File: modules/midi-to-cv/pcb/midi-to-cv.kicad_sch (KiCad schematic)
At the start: 47 parts, among them U2 ATtiny4313-PU

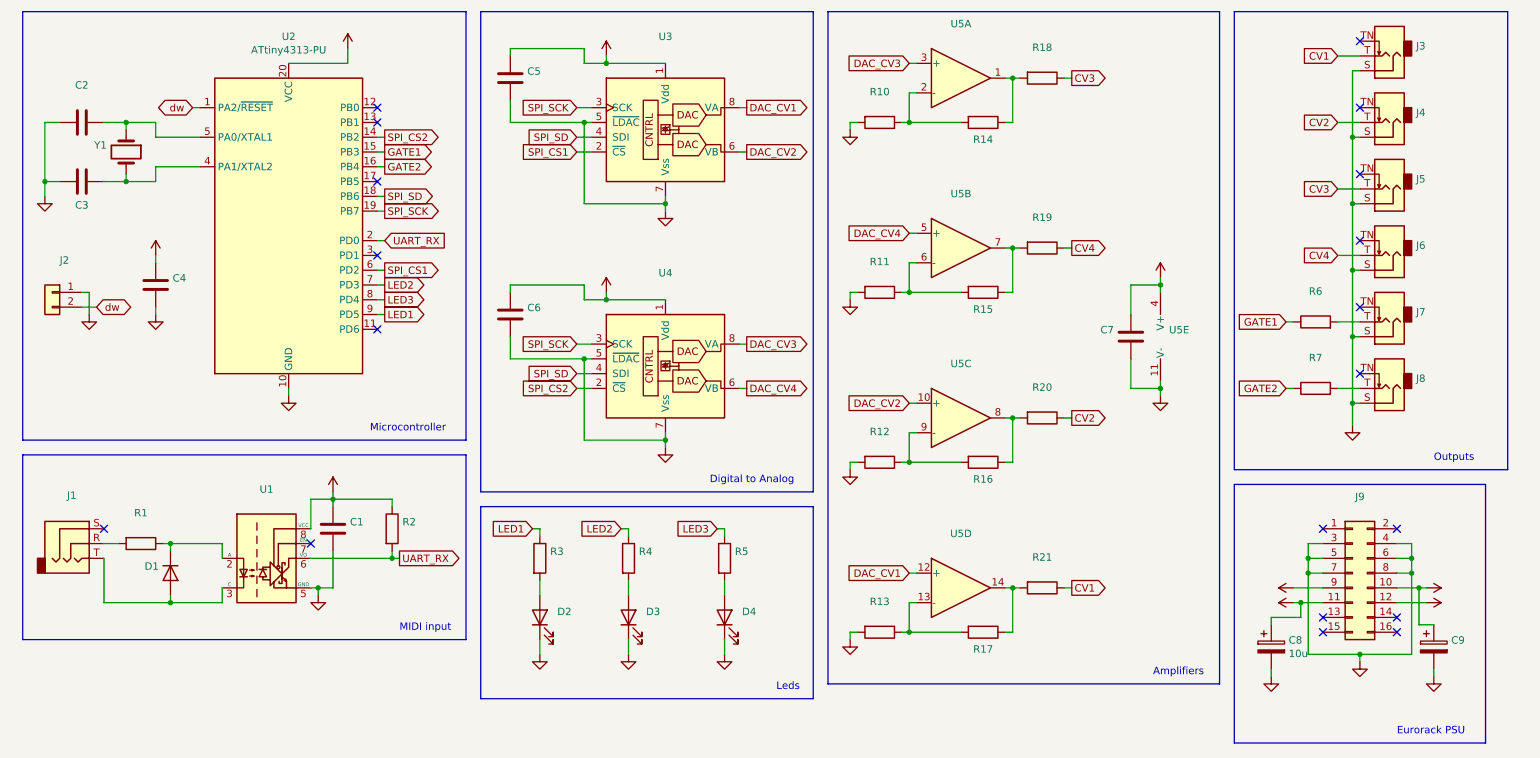
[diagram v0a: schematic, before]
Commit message: modules: midi-to-cv: revision A (redesign)
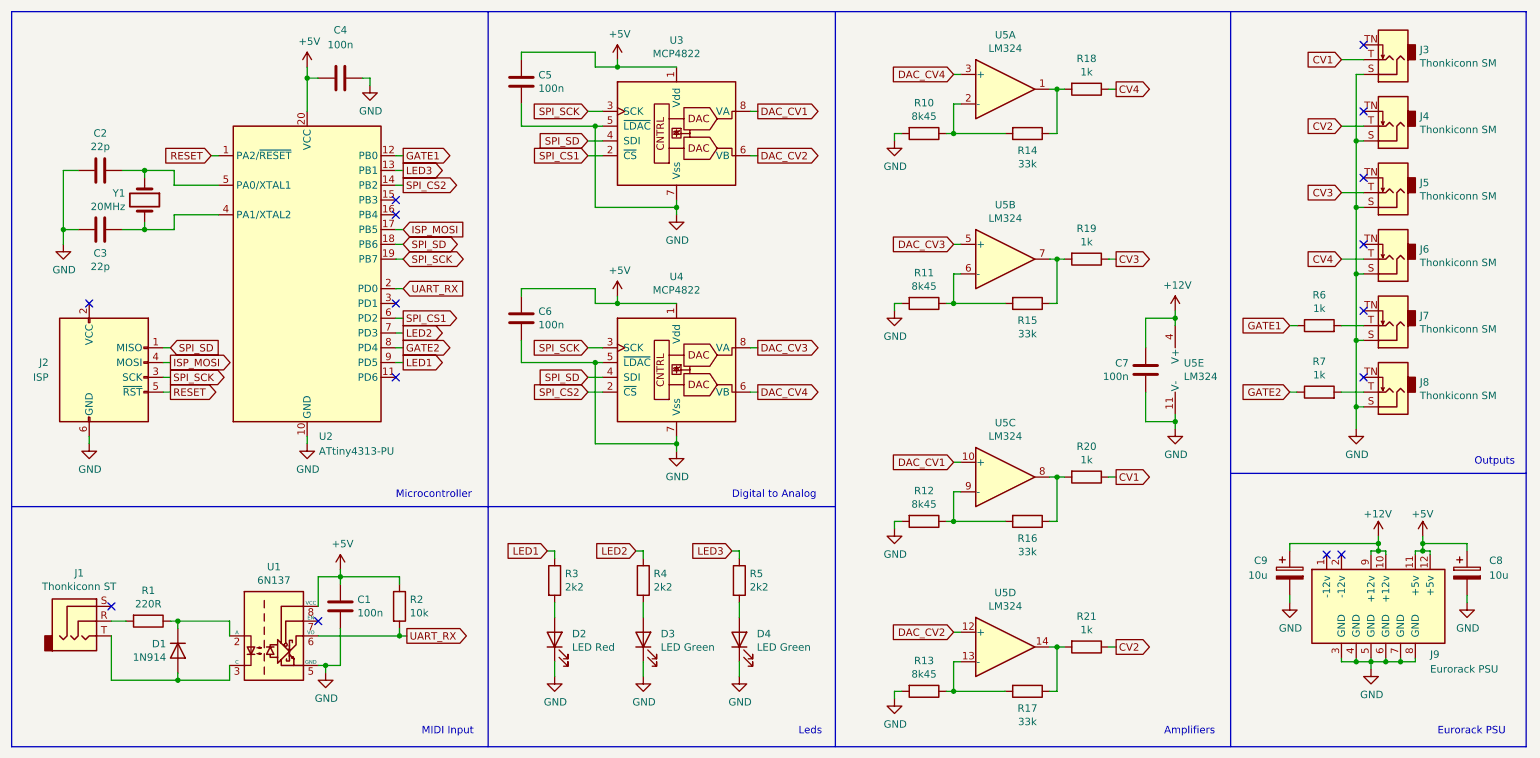
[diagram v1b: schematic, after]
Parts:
- removed J2: (no value), symbol Connector_Generic:Conn_01x02
- removed J9: (no value), symbol Connector_Generic:Conn_02x08_Odd_Even
- added J2: ISP, eurorack:IDC-Header_2x03_P2.54mm_Vertical, symbol Connector:AVR-ISP-6
- added J9: Eurorack PSU, eurorack:IDC-Header_2x08_P2.54mm_Vertical, symbol eurorack:Connector_Eurorack_PSU
- C1, C4, C5, C6, C7: value (none) -> 100n; footprint (none) -> Capacitor_THT:C_Disc_D4.3mm_W1.9mm_P5.00mm
- C2, C3: value (none) -> 22p; footprint (none) -> Capacitor_THT:C_Disc_D3.0mm_W1.6mm_P2.50mm
- C9: value (none) -> 10u; footprint (none) -> Capacitor_THT:CP_Radial_D5.0mm_P2.50mm
- D1: value (none) -> 1N914; footprint (none) -> Diode_THT:D_DO-35_SOD27_P7.62mm_Horizontal
- D2: value (none) -> LED Red; footprint (none) -> LED_THT:LED_D3.0mm
- D3, D4: value (none) -> LED Green; footprint (none) -> LED_THT:LED_D3.0mm
- J1: value (none) -> Thonkiconn ST; footprint (none) -> eurorack:Jack_3.5mm_QingPu_WQP-PJ366ST_Vertical
- J3, J4, J5, J6, J7, J8: value (none) -> Thonkiconn SM; footprint (none) -> eurorack:Jack_3.5mm_QingPu_WQP-PJ398SM_Vertical
- R1: value (none) -> 220R; footprint (none) -> Resistor_THT:R_Axial_DIN0207_L6.3mm_D2.5mm_P10.16mm_Horizontal
- R10, R11, R12, R13: value (none) -> 8k45; footprint (none) -> Resistor_THT:R_Axial_DIN0207_L6.3mm_D2.5mm_P10.16mm_Horizontal
- R14, R15, R16, R17: value (none) -> 33k; footprint (none) -> Resistor_THT:R_Axial_DIN0207_L6.3mm_D2.5mm_P10.16mm_Horizontal
- R18, R19, R20, R21, R6, R7: value (none) -> 1k; footprint (none) -> Resistor_THT:R_Axial_DIN0207_L6.3mm_D2.5mm_P10.16mm_Horizontal
- R2: value (none) -> 10k; footprint (none) -> Resistor_THT:R_Axial_DIN0207_L6.3mm_D2.5mm_P10.16mm_Horizontal
- R3, R4, R5: value (none) -> 2k2; footprint (none) -> Resistor_THT:R_Axial_DIN0207_L6.3mm_D2.5mm_P10.16mm_Horizontal
- U1: value (none) -> 6N137; footprint (none) -> Package_DIP:DIP-8_W7.62mm
- U3, U4: value (none) -> MCP4822; footprint (none) -> Package_DIP:DIP-8_W7.62mm
- U5: value (none) -> LM324; footprint (none) -> Package_DIP:DIP-14_W7.62mm
- Y1: value (none) -> 20MHz; footprint (none) -> Crystal:Crystal_HC49-U_Vertical
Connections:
- net +12V: now also J9.10 (+12v), J9.9 (+12v)
- net +5V: now also J9.11 (+5v), J9.12 (+5v)
- net CV1: now also R20.1; no longer R21.1
- net CV2: now also R21.1; no longer R20.1
- net CV3: now also R19.1; no longer R18.1
- net CV4: now also R18.1; no longer R19.1
- net DAC_CV1: now also U5.10 (+); no longer U5.12 (+)
- net DAC_CV2: now also U5.12 (+); no longer U5.10 (+)
- net DAC_CV3: now also U5.5 (+); no longer U5.3 (+)
- net DAC_CV4: now also U5.3 (+); no longer U5.5 (+)
- net GATE1: now also U2.12 (PB0); no longer U2.15 (PB3)
- net GATE2: now also U2.8 (PD4); no longer U2.16 (PB4)
- net GND: now also J2.6 (GND), J9.3 (GND), J9.4 (GND), J9.5 (GND), J9.6 (GND), J9.7 (GND), J9.8 (GND)
- net LED3: now also U2.13 (PB1); no longer U2.8 (PD4)
- net SPI_SCK: now also J2.3 (SCK)
- net SPI_SD: now also J2.1 (MISO)
- net ISP_MOSI: now reaches U2.17 (PB5)
- net ISP_MOSI: now also J2.4 (MOSI)
- net dw renamed RESET
- net RESET: now also J2.5 (~{RST})
- no-connect marks 19 -> 15
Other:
- note added: "MIDI Input"
- note removed: "MIDI input"
- company: (none) -> eurorack.rgm.io
- moved on the sheet: C1, C2, C3, C4, C5, C6, C7, D1, D2, D3, D4, J1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
